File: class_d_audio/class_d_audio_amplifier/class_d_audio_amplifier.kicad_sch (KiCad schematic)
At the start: 50 parts

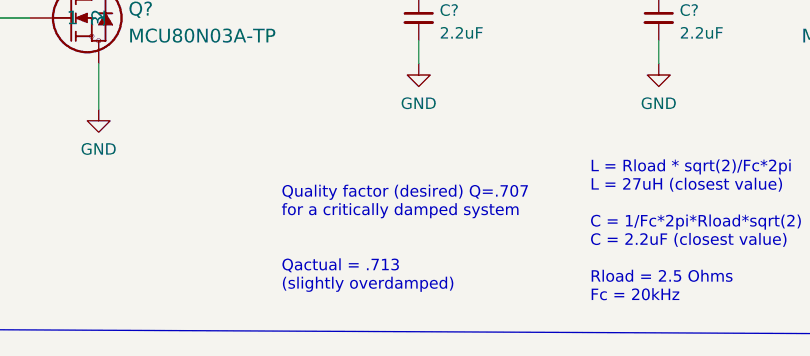
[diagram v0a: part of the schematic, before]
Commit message: correction to quality factor note on LC filter
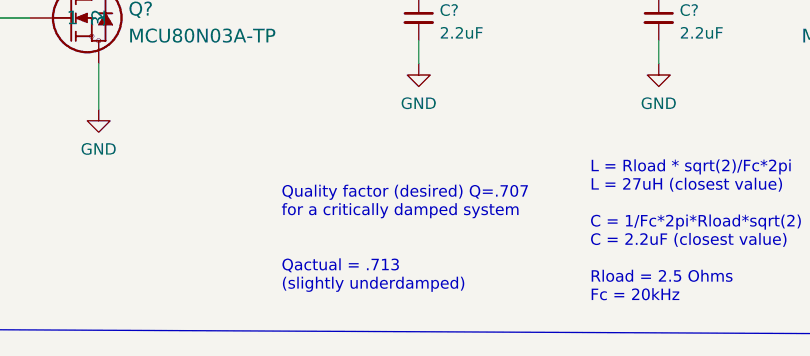
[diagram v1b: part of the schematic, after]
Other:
- note added: "Quality factor (desired) Q=.707 for a critically damped system Qactual = .713 (slightly underdamped)"
- note removed: "Quality factor (desired) Q=.707 for a critically damped system Qactual = .713 (slightly overdamped)"
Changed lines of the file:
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@@
     (effects (font (size 1.27 1.27)) (justify left bottom))
   )
-  (text "Quality factor (desired) Q=.707\nfor a critically damped system\n\n\nQactual = .713\n(slightly overdamped)"
+  (text "Quality factor (desired) Q=.707\nfor a critically damped system\n\n\nQactual = .713\n(slightly underdamped)"
     (at 130.81 257.81 0)
     (effects (font (size 1.27 1.27)) (justify left bottom))

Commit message: completed layout
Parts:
- removed J? (x3): Conn_01x02, symbol Connector_Generic:Conn_01x02
- removed J?: Conn_01x12, symbol Connector_Generic:Conn_01x12
- removed TP? (x2): TP, footprints:tp_1.6mm, symbol formula:TP
- removed TP?: Speaker_Out1, footprints:tp_1.6mm, symbol formula:TP
- added D3, D4: LED_BLUE, Resistor_SMD:R_0805_2012Metric, symbol eclectronics:LED_BLUE
- added J1, J2, J5: Conn_01x02, audio_amplifier:CUI_TB001-500-02BE, symbol audio_amplifier:Conn_01x02
- added J3: Conn_01x07, Connector_PinHeader_2.54mm:PinHeader_1x07_P2.54mm_Vertical, symbol Connector_Generic:Conn_01x07
- added R10, R9: 200, Resistor_SMD:R_0603_1608Metric, symbol audio_amplifier:200
- added TP1, TP2: TP, TestPoint:TestPoint_Pad_D2.0mm, symbol formula:TP
- added TP4: Speaker_Out1, TestPoint:TestPoint_Pad_D3.0mm, symbol formula:TP
- J4: renamed from J?; footprint (none) -> Connector_PinHeader_2.54mm:PinHeader_1x05_P2.54mm_Vertical
- JP1: renamed from JP?; footprint (none) -> Connector_PinHeader_2.54mm:PinHeader_1x02_P2.54mm_Vertical
- TP3: renamed from TP?; footprint footprints:tp_1.6mm -> TestPoint:TestPoint_Pad_D2.0mm
- TP5: renamed from TP?; footprint footprints:tp_1.6mm -> TestPoint:TestPoint_Pad_D3.0mm
- U2: renamed from U?; footprint AP63203WU-7_DIO -> audio_amplifier:AP63203WU-7
- gave numbers to parts that had none: 38
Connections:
- net +12V: now also J1.2 (Pin_2)
- net +5V: now also TP2.1 (TP)
- net GND: now also D3.1, D4.1, J1.1 (Pin_1), J5.2 (Pin_2), TP1.1 (TP); no longer U1.6 (GND), U1.9 (FLAG)
- net PWM_L: now also U3.2 (PWM)
- net RA4: now also J3.2 (Pin_2)
- net RA7: now also J3.1 (Pin_1)
- net RB10: now also J3.4 (Pin_4), R10.1
- net RB11: now also J3.5 (Pin_5), R9.1
- net RB12: now also J3.6 (Pin_6)
- net RB13: now also J3.7 (Pin_7)
- net RB4: now also J3.3 (Pin_3)
- net audio_in: now also J5.1 (Pin_1)
- net speaker+: now also J2.2 (Pin_2), TP4.1 (TP)
- net speaker-: now also J2.1 (Pin_1)
- net at Q1.1: no longer U1.8 (DRVH)
- net at C3.2, L2.1, Q1.3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: no longer U1.7 (SW)
- net at C3.1: no longer U1.1 (BST)
- net at Q2.1: no longer U1.5 (DRVL)
- net RA2: no longer names the net of U4.9 (RA2), Y1.1
- net RA3: no longer names the net of U4.10 (RA3), Y1.3
- new net: D3.2, R9.2
- new net: D4.2, R10.2
- no-connect marks 1 -> 0
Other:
- note added: "Programming LEDs"
- moved on the sheet: U1

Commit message: modified parts library and exported bom
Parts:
- J3: MPN (none) -> PPTC071LFBN-RC
- J4: MPN (none) -> RS1-05-G
- Q1, Q2, Q3, Q4: MPN (none) -> MCU80N03A-TP
- U1, U3: MPN (none) -> NCP81151MNTBG
- U2: MPN (none) -> AP63205WU-7
- U4: MPN (none) -> PIC24FV16KM202-I/SP
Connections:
- net GND: now also U1.6 (GND), U1.9 (FLAG)
- net at Q1.1: now also U1.8 (DRVH)
- net at C3.2, L2.1, Q1.3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: now also U1.7 (SW)
- net at C3.1: now also U1.1 (BST)
- net at Q2.1: now also U1.5 (DRVL)
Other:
- moved on the sheet: U1
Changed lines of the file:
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@@
     (stroke (width 0) (type default) (color 0 0 0 0))
   )
+  (wire (pts (xy 93.98 215.9) (xy 97.79 215.9))
+    (stroke (width 0) (type default) (color 0 0 0 0))
+  )
   (wire (pts (xy 381 57.15) (xy 384.81 57.15))
     (stroke (width 0) (type default) (color 0 0 0 0))
@@
     (stroke (width 0) (type default) (color 0 0 0 0))
   )
-  (wire (pts (xy 118.11 48.26) (xy 118.11 55.88))
+  (wire (pts (xy 93.98 227.33) (xy 102.87 227.33))
     (stroke (width 0) (type default) (color 0 0 0 0))
   )
-  (wire (pts (xy 93.98 215.9) (xy 97.79 215.9))
+  (wire (pts (xy 118.11 48.26) (xy 118.11 55.88))
     (stroke (width 0) (type default) (color 0 0 0 0))
   )
@@
     (stroke (width 0) (type default) (color 0 0 0 0))
   )
+  (wire (pts (xy 93.98 223.52) (xy 97.79 223.52))
+    (stroke (width 0) (type default) (color 0 0 0 0))
+  )
   (wire (pts (xy 331.47 64.77) (xy 350.52 64.77))
     (stroke (width 0) (type default) (color 0 0 0 0))
@@
     (stroke (width 0) (type default) (color 0 0 0 0))
   )
-  (wire (pts (xy 93.98 227.33) (xy 102.87 227.33))
-    (stroke (width 0) (type default) (color 0 0 0 0))
-  )
   (wire (pts (xy 265.43 33.02) (xy 269.24 33.02))
     (stroke (width 0) (type default) (color 0 0 0 0))
@@
     (stroke (width 0) (type default) (color 0 0 0 0))
   )
+  (wire (pts (xy 93.98 212.09) (xy 102.87 212.09))
+    (stroke (width 0) (type default) (color 0 0 0 0))
+  )
   (wire (pts (xy 96.52 106.68) (xy 113.03 106.68))
     (stroke (width 0) (type default) (color 0 0 0 0))
@@
     (stroke (width 0) (type default) (color 0 0 0 0))
   )
-  (wire (pts (xy 93.98 212.09) (xy 102.87 212.09))
-    (stroke (width 0) (type default) (color 0 0 0 0))
-  )
   (polyline (pts (xy 294.64 262.89) (xy 294.64 182.88))
     (stroke (width 0) (type default) (color 0 0 0 0))
@@
     (stroke (width 0) (type default) (color 0 0 0 0))
   )
-  (wire (pts (xy 93.98 223.52) (xy 97.79 223.52))
-    (stroke (width 0) (type default) (color 0 0 0 0))
-  )
   (wire (pts (xy 68.58 50.8) (xy 68.58 40.64))
     (stroke (width 0) (type default) (color 0 0 0 0))
@@
     (pin "1")
   )
-  (symbol (lib_name "NCP81151MNTBG_1") (lib_id "audio_amplifier:NCP81151MNTBG") (at 257.81 212.09 0) (mirror y) (unit 1)
+  (symbol (lib_id "audio_amplifier:NCP81151MNTBG") (at 257.81 212.09 0) (mirror y) (unit 1)
     (in_bom yes) (on_board yes) (fields_autoplaced)
     (property "Reference" "U3" (id 0) (at 241.3 204.1197 0)
@@
       (effects (font (size 1.524 1.524)) hide)
     )
+    (property "MPN" "NCP81151MNTBG" (id 4) (at 257.81 212.09 0)
+      (effects (font (size 1.27 1.27)) hide)
+    )
     (pin "1")
     (pin "2")
@@
       (effects (font (size 1.27 1.27)) hide)
     )
+    (property "MPN" "PIC24FV16KM202-I/SP" (id 5) (at 280.67 35.56 0)
+      (effects (font (size 1.27 1.27)) hide)
+    )
     (pin "1")
     (pin "10")
@@
       (effects (font (size 1.524 1.524)) hide)
     )
+    (property "MPN" "MCU80N03A-TP" (id 4) (at 102.87 212.09 0)
+      (effects (font (size 1.27 1.27)) hide)
+    )
     (pin "1")
     (pin "2")
@@
       (effects (font (size 1.27 1.27)) hide)
     )
+    (property "MPN" "RS1-05-G" (id 4) (at 62.23 154.94 0)
+      (effects (font (size 1.27 1.27)) hide)
+    )
     (pin "1")
     (pin "2")
@@
     (pin "1")
   )
-  (symbol (lib_id "audio_amplifier:MCU80N03A-TP") (at 102.87 227.33 0) (unit 1)
+  (symbol (lib_name "MCU80N03A-TP_3") (lib_id "audio_amplifier:MCU80N03A-TP") (at 102.87 227.33 0) (unit 1)
     (in_bom yes) (on_board yes) (fields_autoplaced)
     (property "Reference" "Q2" (id 0) (at 113.792 226.3538 0)
@@
       (effects (font (size 1.524 1.524)) hide)
     )
+    (property "MPN" "MCU80N03A-TP" (id 4) (at 102.87 227.33 0)
+      (effects (font (size 1.27 1.27)) hide)
+    )
     (pin "1")
     (pin "2")
@@
     (pin "1")
   )
-  (symbol (lib_id "audio_amplifier:MCU80N03A-TP") (at 215.9 227.33 0) (mirror y) (unit 1)
+  (symbol (lib_name "MCU80N03A-TP_1") (lib_id "audio_amplifier:MCU80N03A-TP") (at 215.9 227.33 0) (mirror y) (unit 1)
     (in_bom yes) (on_board yes) (fields_autoplaced)
     (property "Reference" "Q4" (id 0) (at 204.978 226.3538 0)
@@
       (effects (font (size 1.524 1.524)) hide)
     )
+    (property "MPN" "MCU80N03A-TP" (id 4) (at 215.9 227.33 0)
+      (effects (font (size 1.27 1.27)) hide)
+    )
     (pin "1")
     (pin "2")
@@
     (pin "2")
   )
-  (symbol (lib_name "NCP81151MNTBG_1") (lib_id "audio_amplifier:NCP81151MNTBG") (at 60.96 212.09 0) (mirror y) (unit 1)
+  (symbol (lib_name "NCP81151MNTBG_1") (lib_id "audio_amplifier:NCP81151MNTBG") (at 60.96 212.09 0) (unit 1)
     (in_bom yes) (on_board yes) (fields_autoplaced)
-    (property "Reference" "U1" (id 0) (at 44.45 204.1197 0)
+    (property "Reference" "U1" (id 0) (at 77.47 204.1197 0)
       (effects (font (size 1.524 1.524)))
     )
-    (property "Value" "NCP81151MNTBG" (id 1) (at 44.45 207.1131 0)
+    (property "Value" "NCP81151MNTBG" (id 1) (at 77.47 207.1131 0)
       (effects (font (size 1.524 1.524)))
     )
-    (property "Footprint" "audio_amplifier:NCP81151MNTBG" (id 2) (at 40.64 205.994 0)
+    (property "Footprint" "audio_amplifier:NCP81151MNTBG" (id 2) (at 81.28 205.994 0)
       (effects (font (size 1.524 1.524)) hide)
     )
@@
       (effects (font (size 1.524 1.524)) hide)
     )
+    (property "MPN" "NCP81151MNTBG" (id 4) (at 60.96 212.09 0)
+      (effects (font (size 1.27 1.27)) hide)
+    )
     (pin "1")
     (pin "2")
@@
       (effects (font (size 1.27 1.27)) hide)
     )
+    (property "MPN" "AP63205WU-7" (id 5) (at 69.85 41.91 0))
     (pin "1")
     (pin "2")
@@
     (pin "2")
   )
-  (symbol (lib_id "audio_amplifier:MCU80N03A-TP") (at 215.9 212.09 0) (mirror y) (unit 1)
+  (symbol (lib_name "MCU80N03A-TP_2") (lib_id "audio_amplifier:MCU80N03A-TP") (at 215.9 212.09 0) (mirror y) (unit 1)
     (in_bom yes) (on_board yes) (fields_autoplaced)
     (property "Reference" "Q3" (id 0) (at 204.978 211.1138 0)
@@
       (effects (font (size 1.524 1.524)) hide)
     )
+    (property "MPN" "MCU80N03A-TP" (id 4) (at 215.9 212.09 0)
+      (effects (font (size 1.27 1.27)) hide)
+    )
     (pin "1")
     (pin "2")
@@
       (effects (font (size 1.27 1.27)) hide)
     )
+    (property "MPN" "PPTC071LFBN-RC" (id 4) (at 62.23 115.57 0)
+      (effects (font (size 1.27 1.27)) hide)
+    )
